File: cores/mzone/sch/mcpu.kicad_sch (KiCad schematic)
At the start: 36 parts

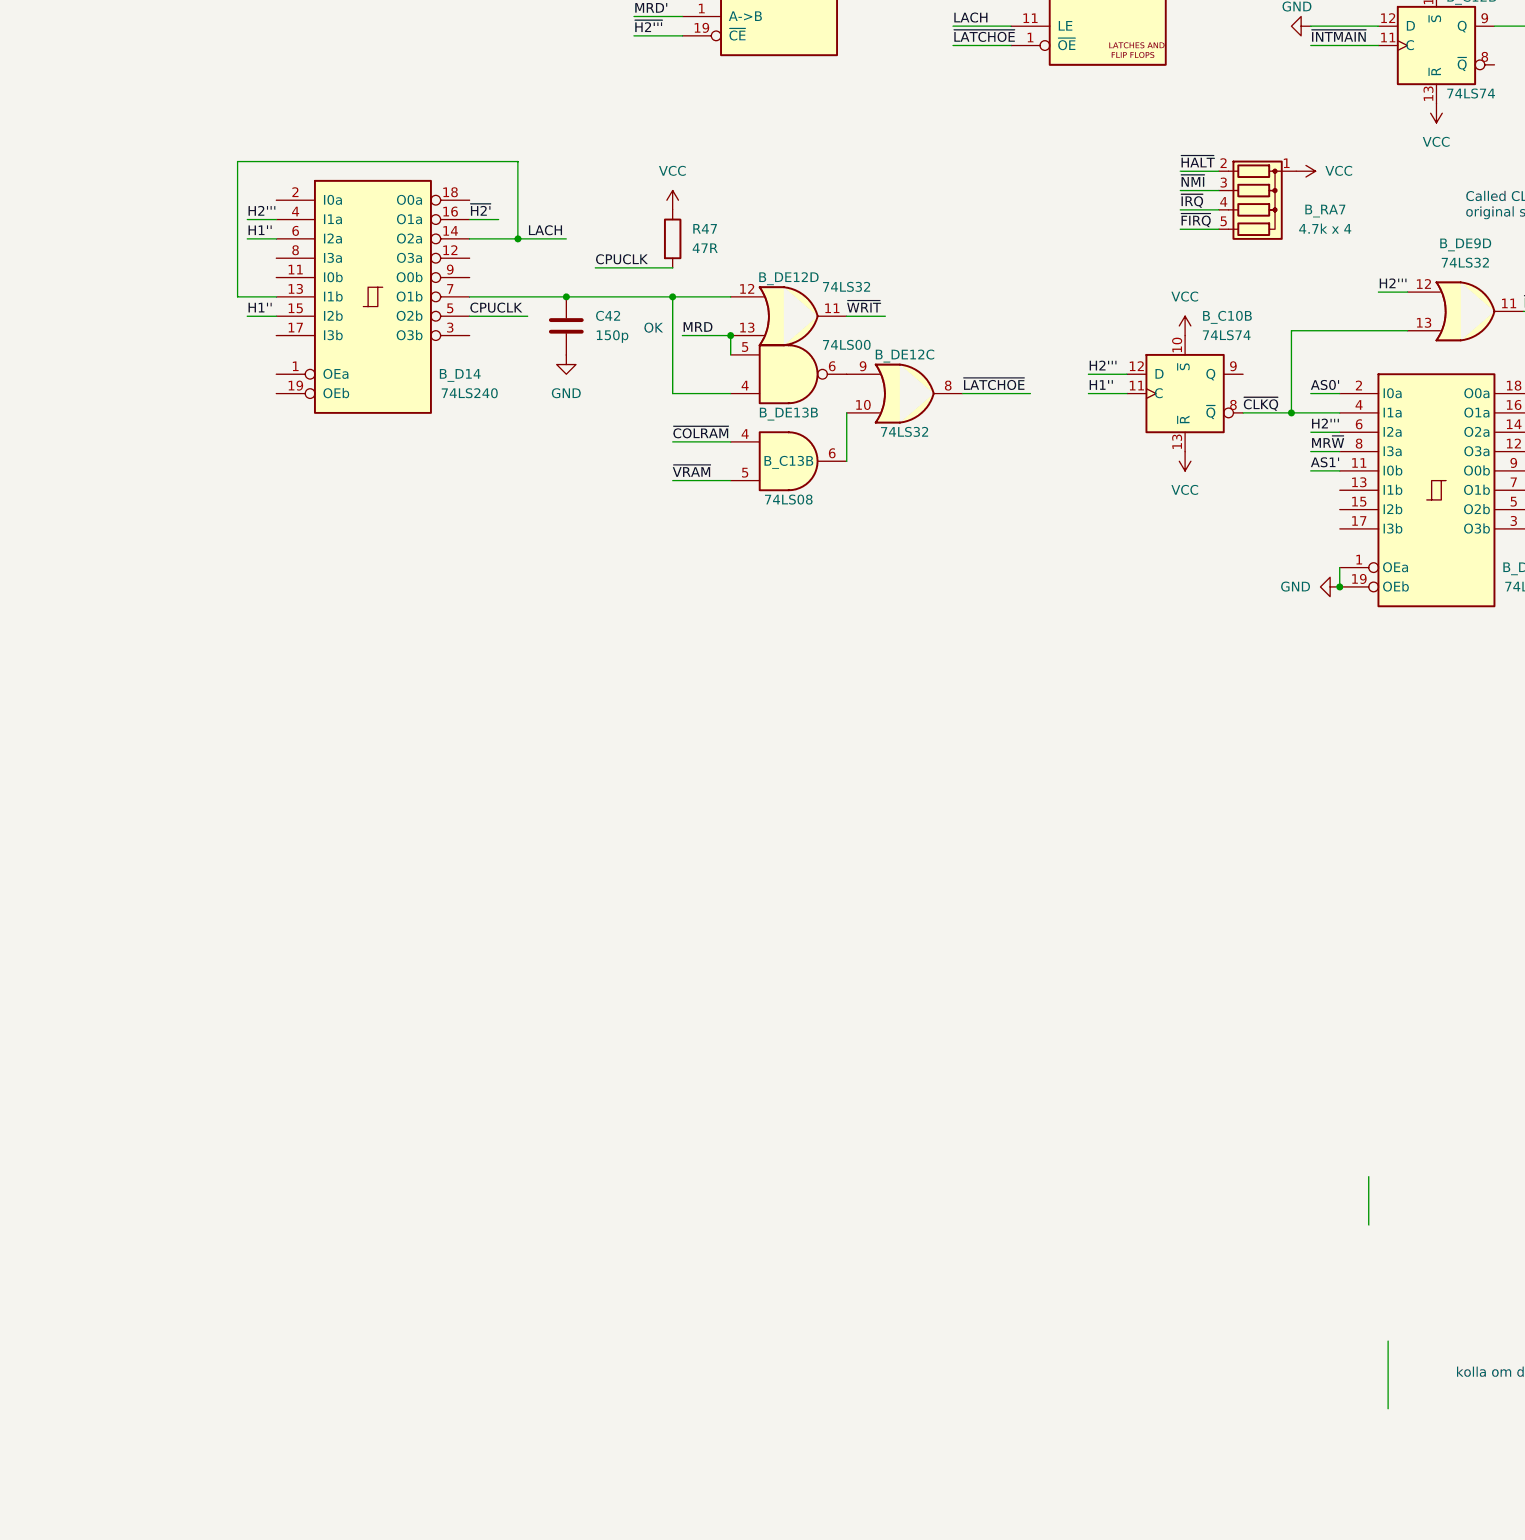
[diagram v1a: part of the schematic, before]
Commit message: mzone core
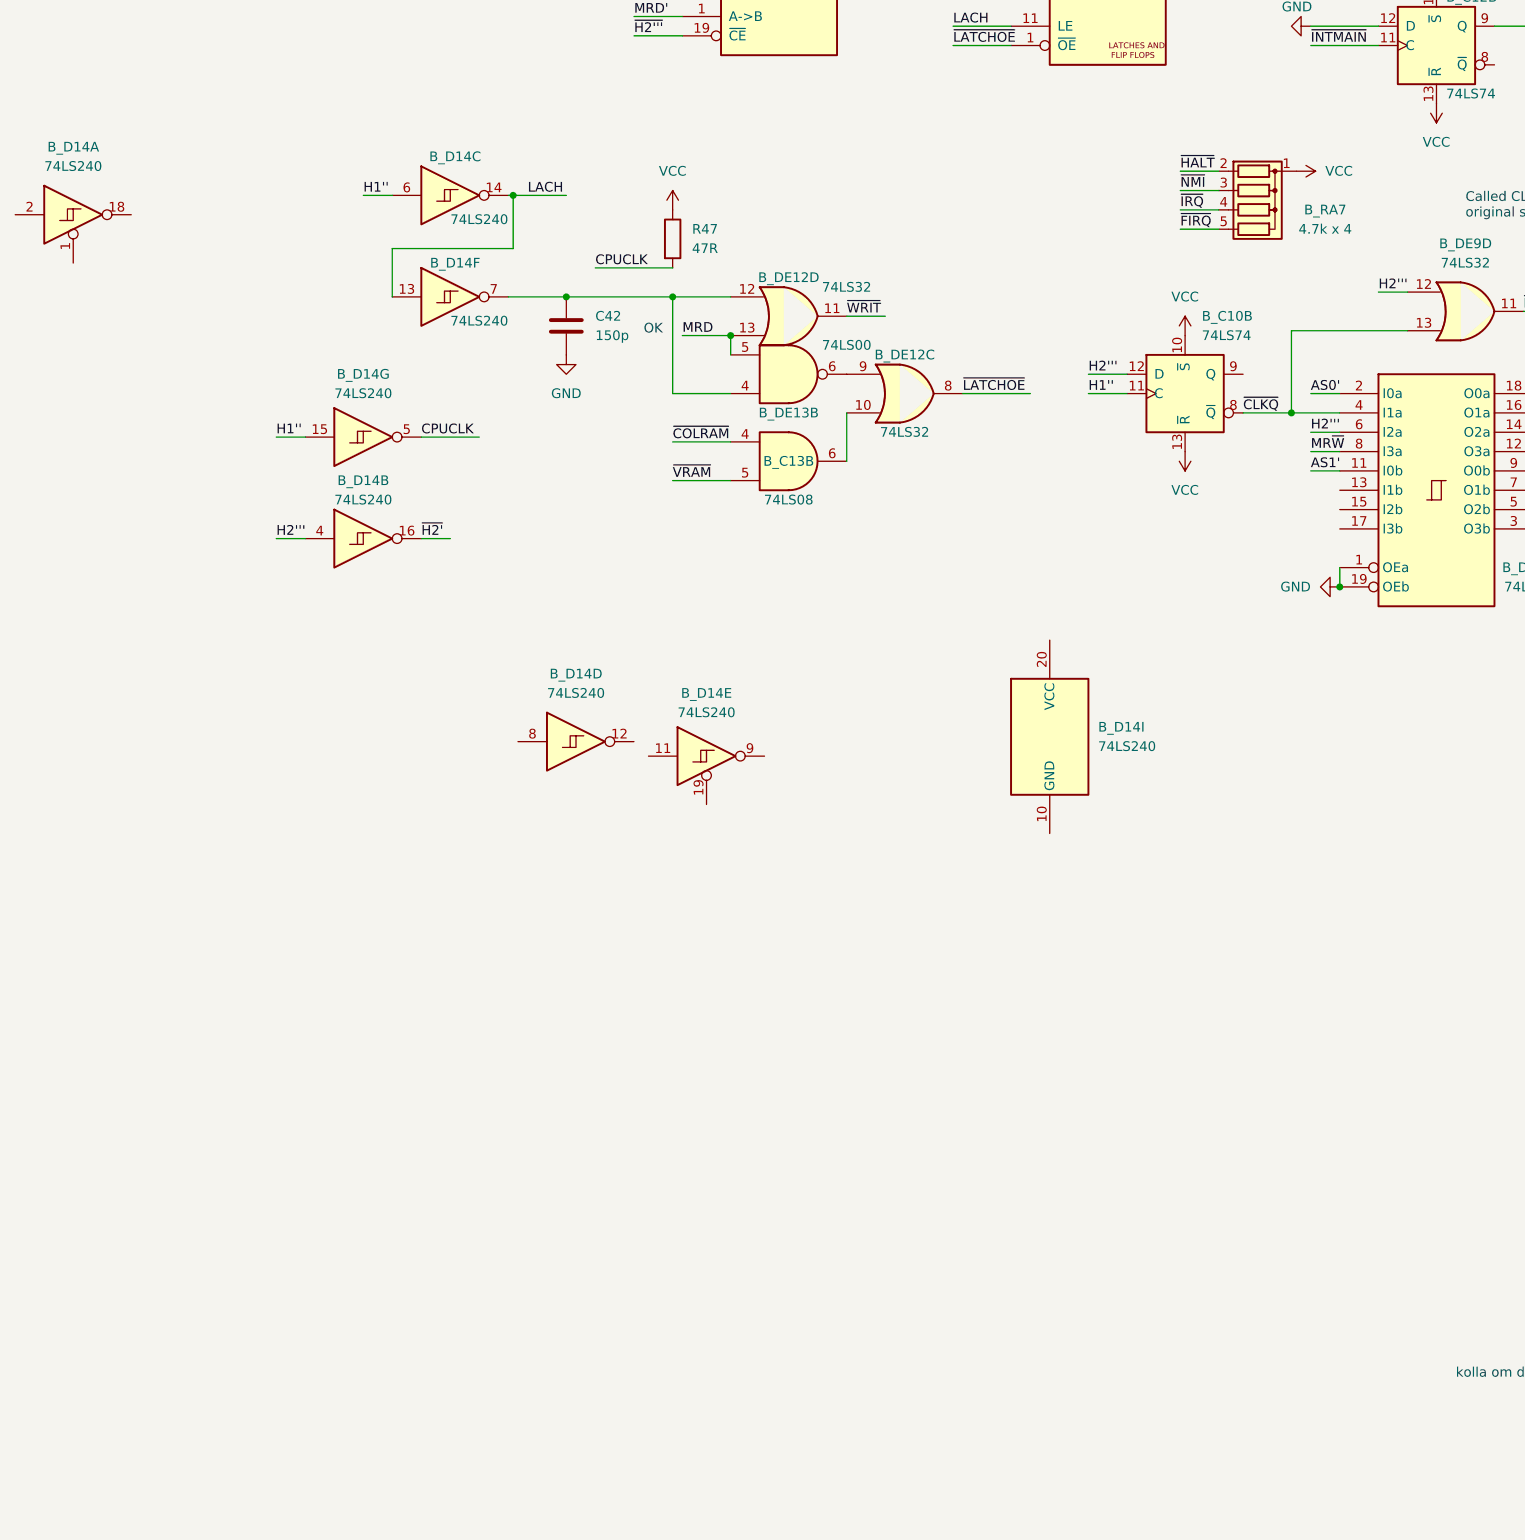
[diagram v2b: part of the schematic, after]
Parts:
- removed B_D14: 74LS240, symbol jt74:74LS240
- added B_D14: 74LS240, symbol 74xx:74LS240_Split
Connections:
- net CPUCLK: now also B_D14.5
- net H1'': now also B_D14.15, B_D14.6
- net H2''': now also B_D14.4
- net LACH: now also B_D14.13, B_D14.14
- net ~{H2'}: now also B_D14.16
- net at B_DE12.12, B_DE13.4, C42.1: now also B_D14.7

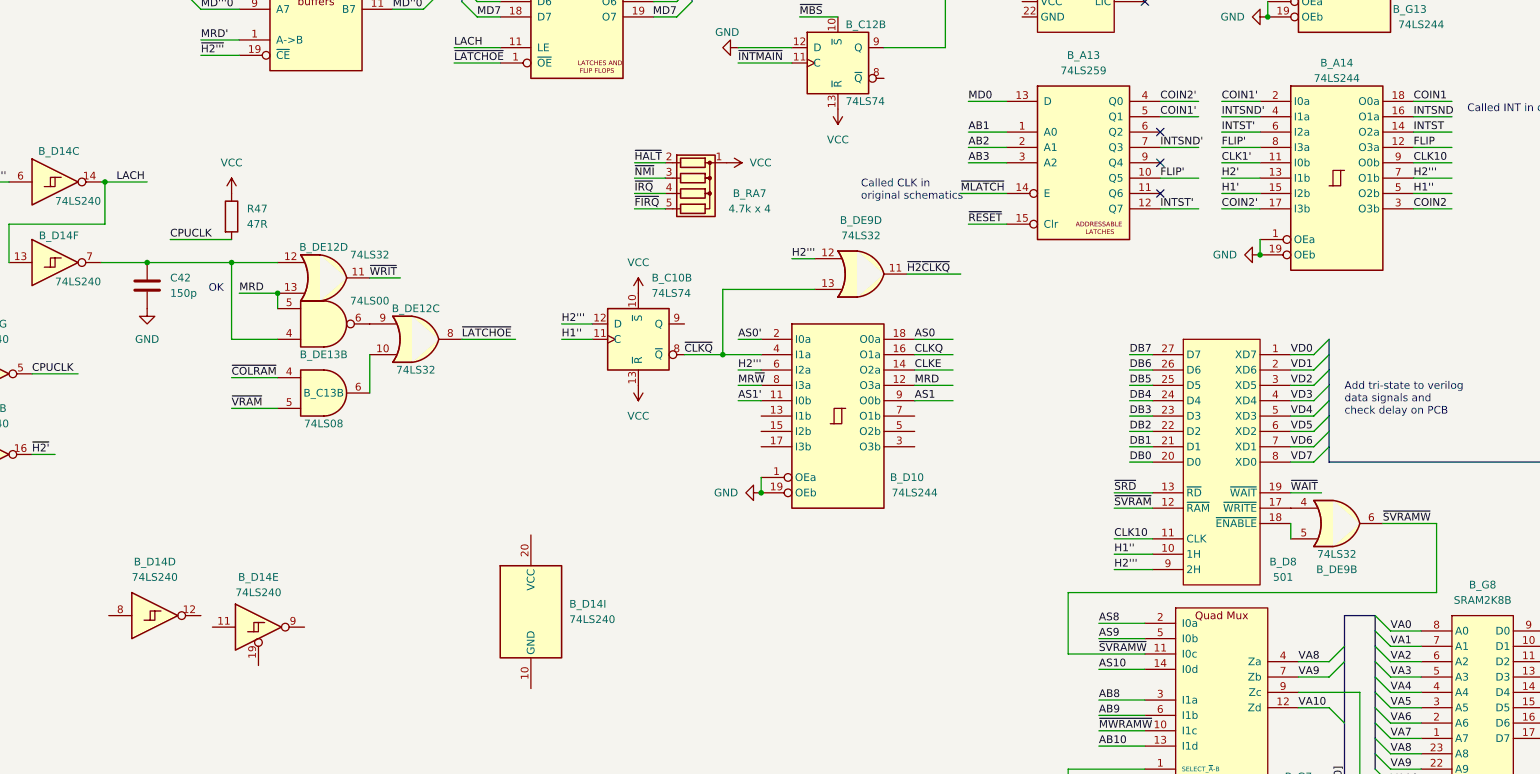
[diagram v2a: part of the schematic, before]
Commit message: mzone core
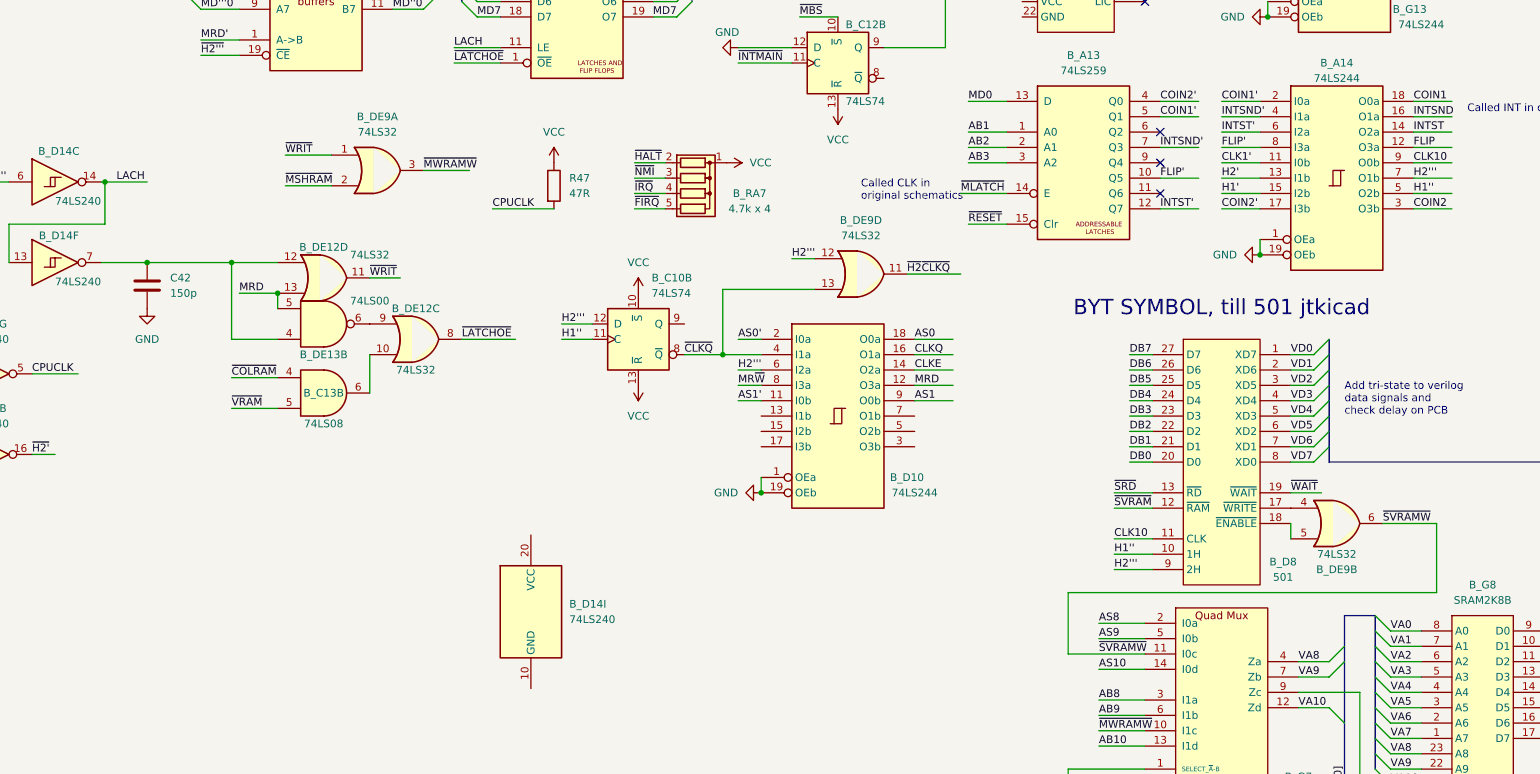
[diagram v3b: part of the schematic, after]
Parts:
- removed unit 5 of B_D14
- removed unit 4 of B_D14
- added unit 1 of B_DE9
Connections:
- net ~{MSHRAM}: now also B_DE9.2
- net ~{MWRAMW}: now also B_DE9.3
- net ~{WRIT}: now also B_DE9.1
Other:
- note added: "BYT SYMBOL, till 501 jtkicad"
- note removed: "OK"
- moved on the sheet: R47
